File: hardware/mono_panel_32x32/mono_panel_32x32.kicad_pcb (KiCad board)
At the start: 2 copper layers, 166.7 x 166.7 mm, 1026 parts

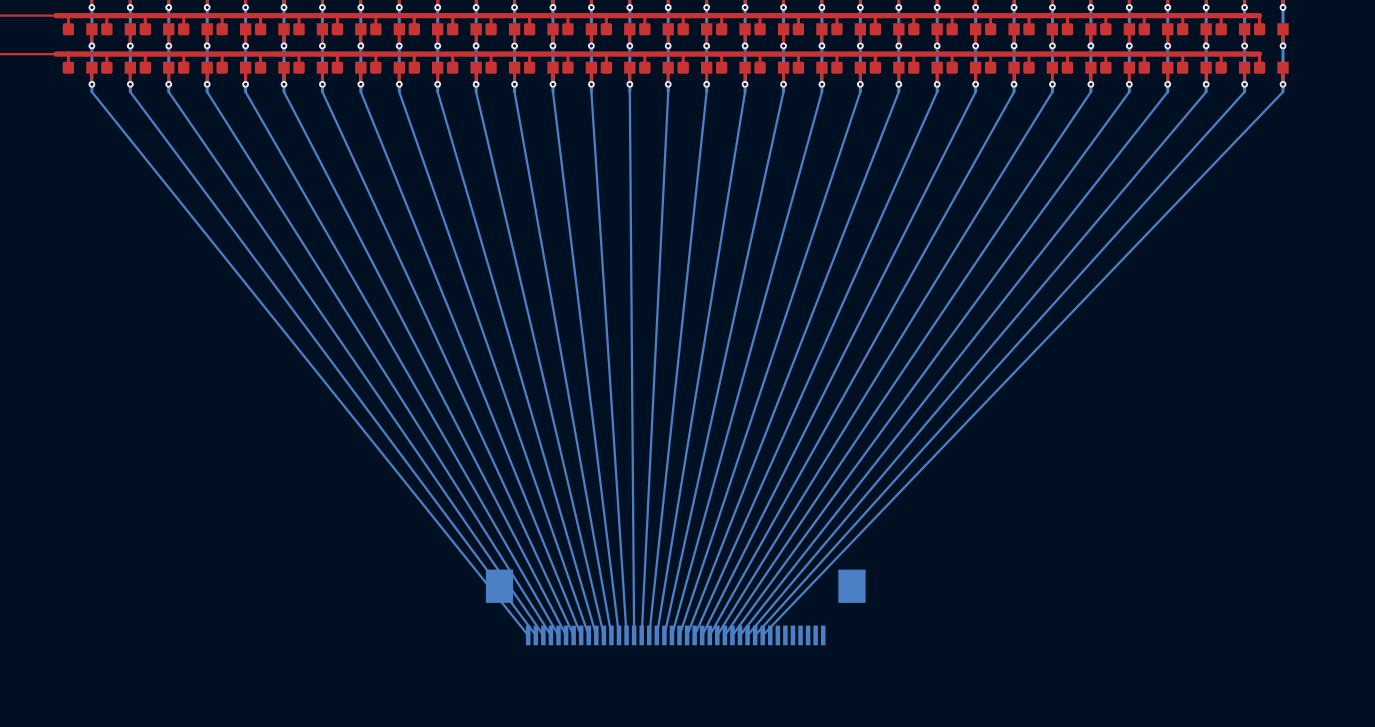
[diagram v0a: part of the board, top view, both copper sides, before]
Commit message: Fix mono panel fan-in DRC and spacious electronics placement.
Route rows through a U-turn via row and drop columns onto FFC pad centerlines so both LED panels are geometrically DRC-clean. Widen the electronics board, clear courtyards and silk, and record the fan-in constraints in cursor.md.

Co-authored-by: illiapliukhin <illiapliukhin@users.noreply.github.com>
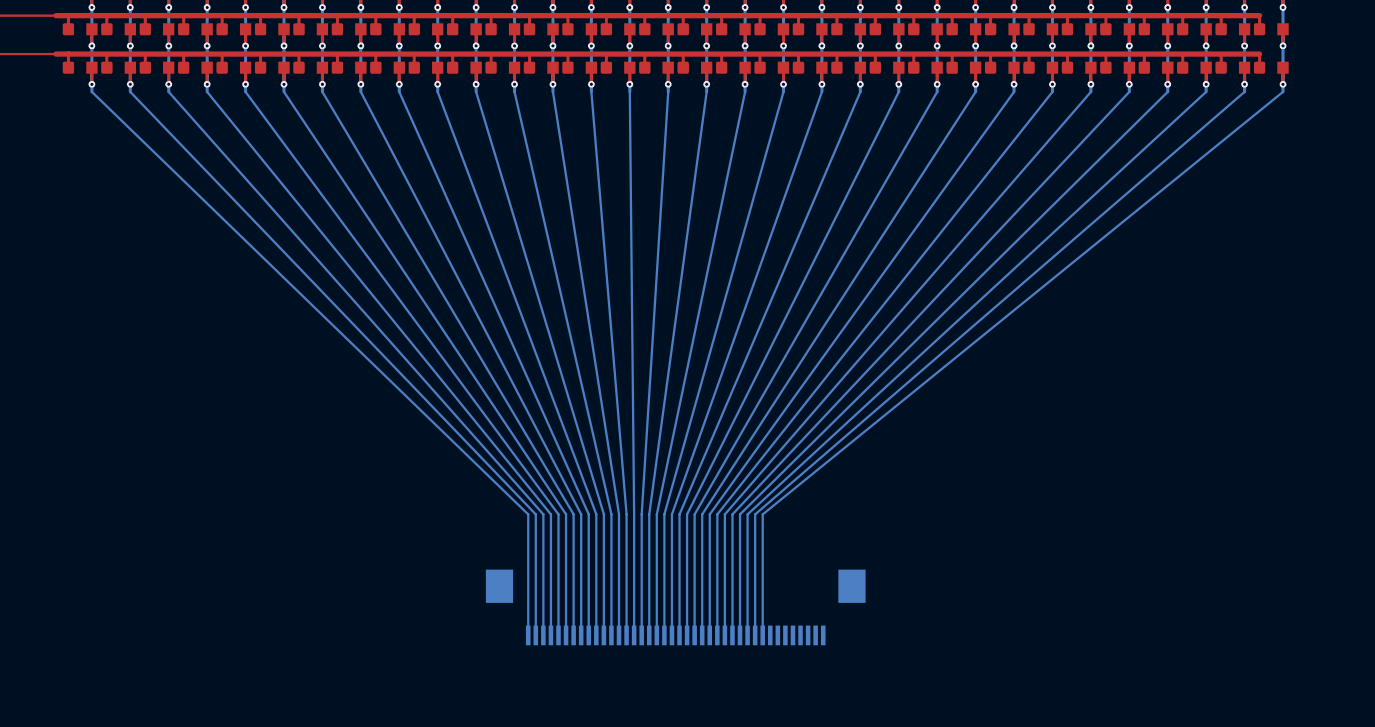
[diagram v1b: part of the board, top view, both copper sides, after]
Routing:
- net COL_32: track 164.2 -> 166.7 mm
- net COL_31: track 162.8 -> 165.2 mm
- net COL_30: track 161.5 -> 163.7 mm
- net COL_01: track 160.5 -> 162.6 mm
- net COL_29: track 160.2 -> 162.2 mm
- net COL_02: track 159.3 -> 161.2 mm
- net COL_28: track 158.9 -> 160.8 mm
- net COL_03: track 158.1 -> 159.8 mm
- net COL_27: track 157.8 -> 159.4 mm
- net COL_04: track 157.0 -> 158.4 mm
- net COL_26: track 156.7 -> 158.1 mm
- net COL_05: track 155.9 -> 157.2 mm
- net COL_25: track 155.6 -> 156.9 mm
- net COL_06: track 154.9 -> 156.0 mm
- net COL_24: track 154.7 -> 155.7 mm
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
